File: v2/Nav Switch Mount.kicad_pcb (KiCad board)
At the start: 2 copper layers, 22.9 x 13.1 mm, 17 parts, among them J1 Conn_01x06, J2 Conn_01x01_Pin, J3 Conn_01x01_Pin, U1 SKQUAAA010

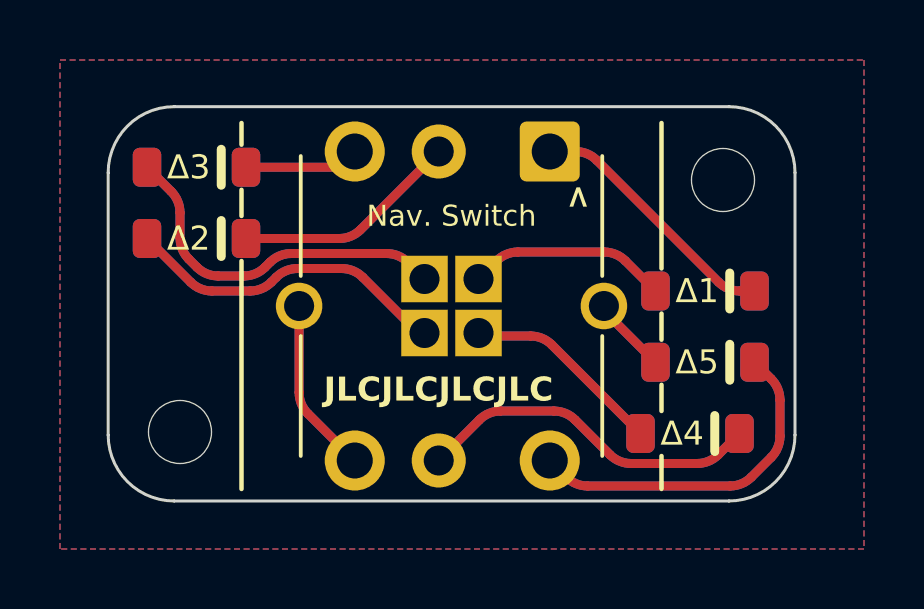
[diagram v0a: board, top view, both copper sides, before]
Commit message: Remove order number
Cost is no different for a board this small!
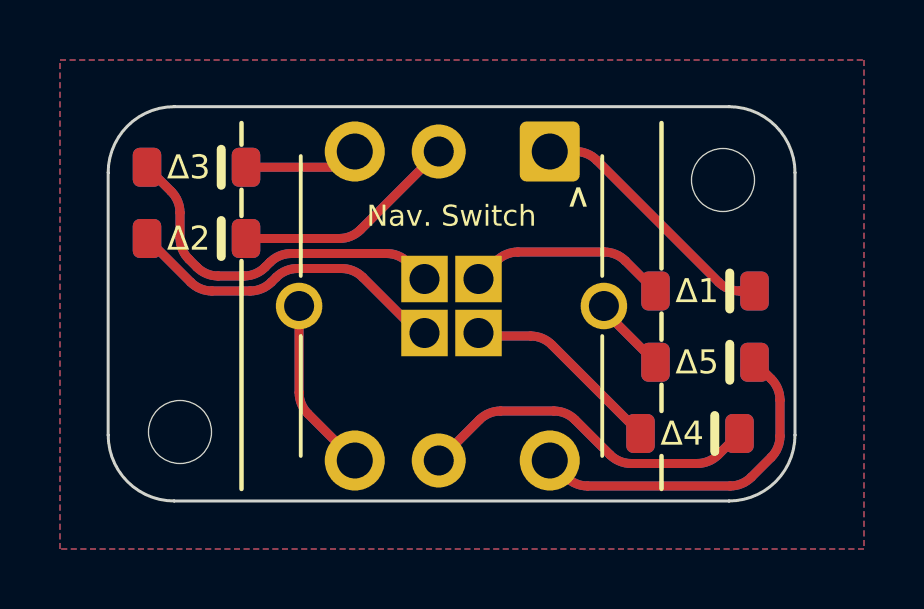
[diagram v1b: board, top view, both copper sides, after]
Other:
- board text removed: "JLCJLCJLCJLC"
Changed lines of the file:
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@@
     (fp_line (start 1 5.025) (end 5 5.025)
       (stroke (width 0.127) (type solid)) (layer "F.SilkS"))
-    (pad "1" thru_hole roundrect (at -5.15 -3.275 270) (size 2 2) (drill 1.2) (layers "*.Cu" "*.Mask") (roundrect_rratio 0.1136363636)
+    (pad "1" thru_hole roundrect (at -5.15 -3.275 270) (size 2 2) (drill 1.2) (layers "*.Cu" "*.Mask") (roundrect_rratio 0.1136365)
       (net 2 "A") (pinfunction "A1") (pintype "bidirectional") (solder_mask_margin 0.102))
     (pad "2" thru_hole circle (at -5.15 0.425 270) (size 1.8 1.8) (drill 1) (layers "*.Cu" "*.Mask")
@@
     (effects (font (size 0.8 0.8) (thickness 0.2) bold))
   )
-  (gr_text "JLCJLCJLCJLC" (at 154.790714 55.25) (layer "F.SilkS")
-    (effects (font (size 0.8 0.8) (thickness 0.15) bold) (justify left bottom))
-  )
   (gr_text "bgkendall\nv2.0" (at 148.25 53.7) (layer "B.Mask")
